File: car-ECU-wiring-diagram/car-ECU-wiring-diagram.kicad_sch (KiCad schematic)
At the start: 29 parts

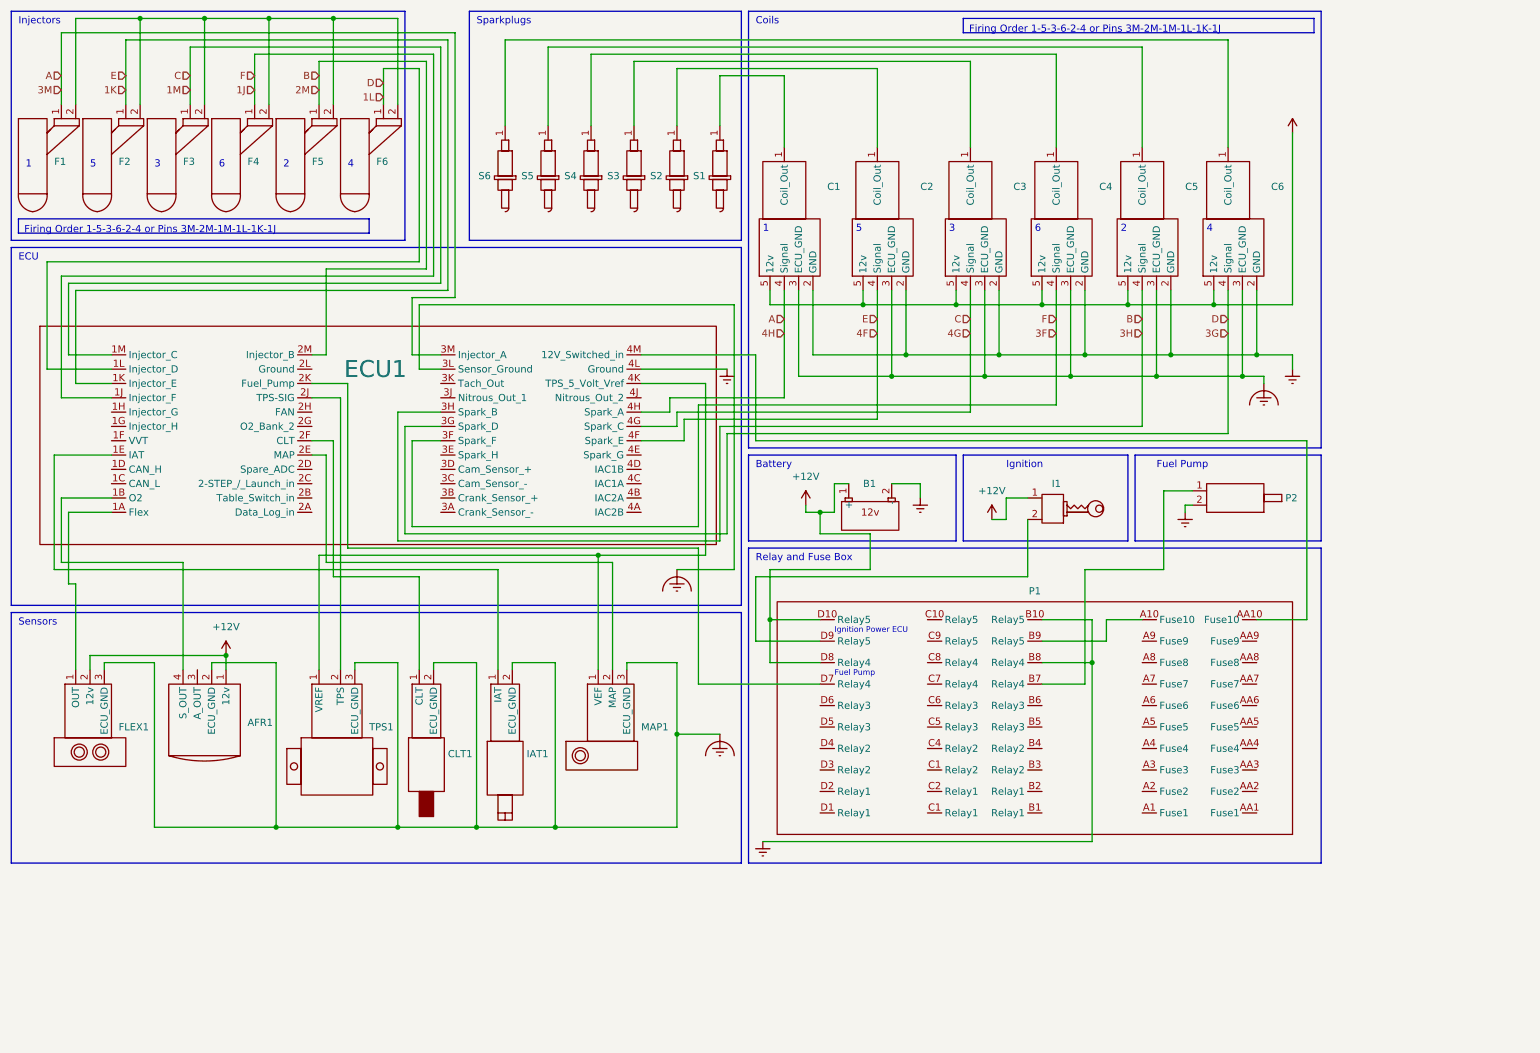
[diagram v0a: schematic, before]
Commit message: Update ECU wiring diagram with corrected pin UUIDs
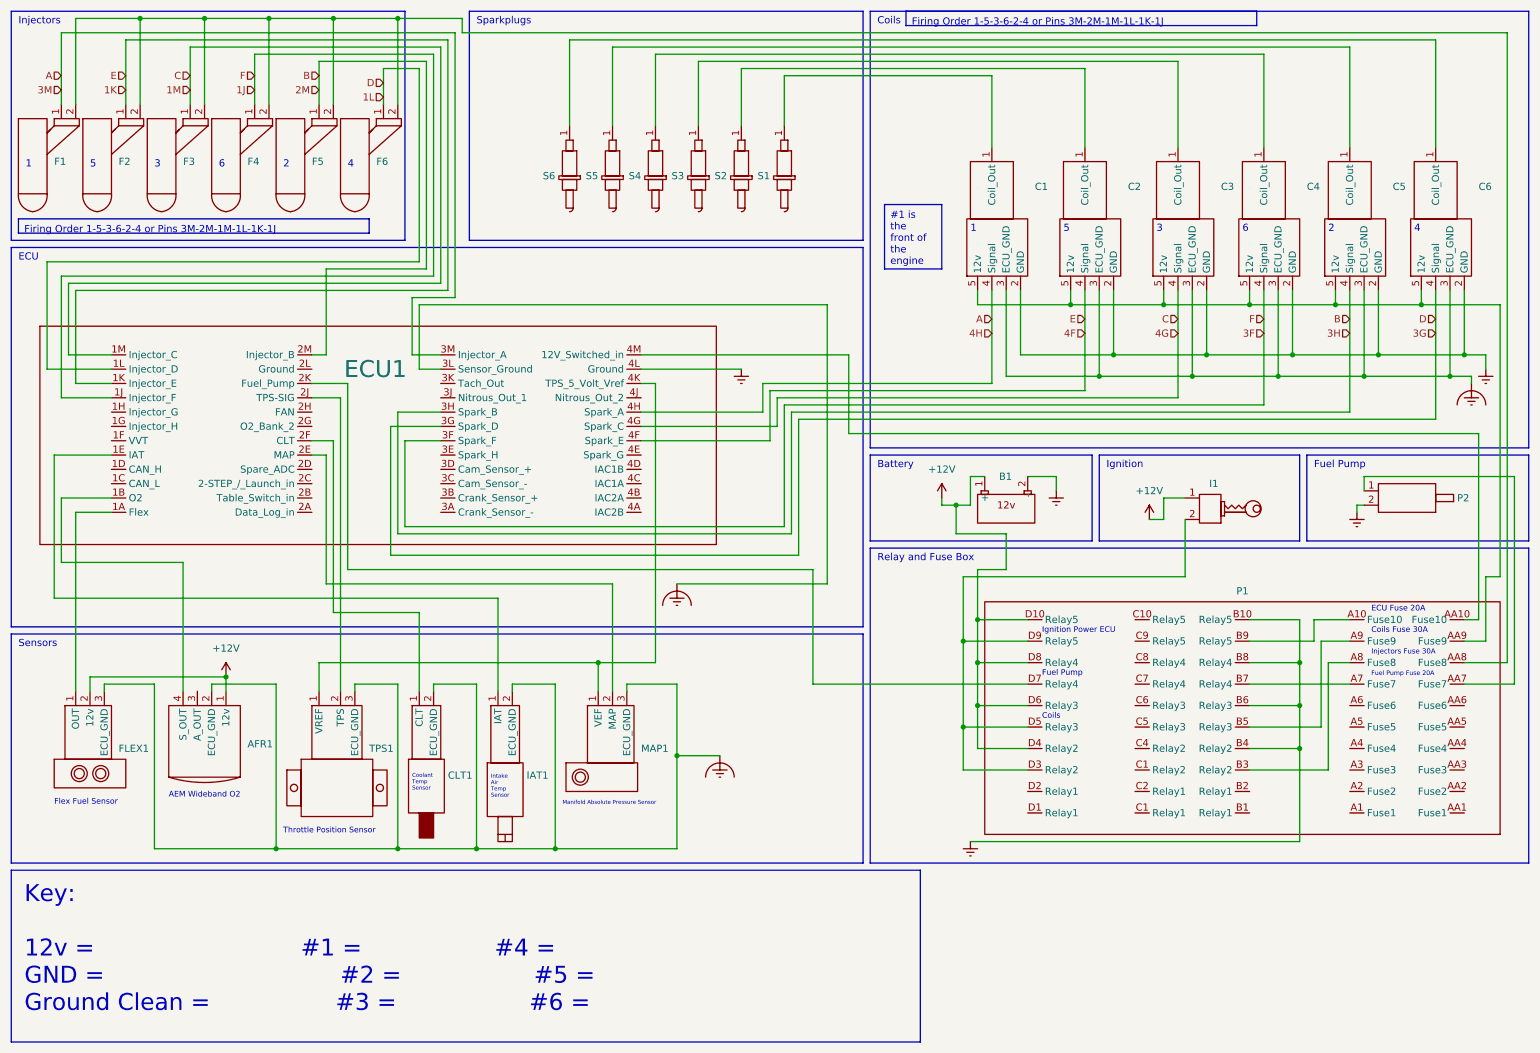
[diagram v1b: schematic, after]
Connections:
- net +12V: now also P1.D4 (Relay2), P1.D6 (Relay3); no longer C1.5 (12v), C2.5 (12v), C3.5 (12v), C4.5 (12v), C5.5 (12v), C6.5 (12v)
- net Earth: now also P1.B4 (Relay2), P1.B6 (Relay3)
- net at F1.2, F2.2, F3.2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: now also P1.AA8 (Fuse8)
- net at I1.2, P1.D9 (Relay5): now also P1.D3 (Relay2), P1.D5 (Relay3)
- net at P2.1: now also P1.AA7 (Fuse7); no longer P1.B7 (Relay4)
- net at P1.A7 (Fuse7): now also P1.B7 (Relay4)
- net at P1.A8 (Fuse8): now also P1.B3 (Relay2)
- net at P1.A9 (Fuse9): now also P1.B5 (Relay3)
- net at P1.AA9 (Fuse9): now also C1.5 (12v), C2.5 (12v), C3.5 (12v), C4.5 (12v), C5.5 (12v), C6.5 (12v)
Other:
- note added: "AEM Wideband O2"
- note added: "Coils Fuse 30A"
- note added: "Coolant Temp Sensor"
- note added: "ECU Fuse 20A"
- note added: "Flex Fuel Sensor"
- note added: "Fuel Pump Fuse 20A"
- note added: "Injectors Fuse 30A"
- note added: "Intake Air Temp Sensor"
- note added: "Manifold Absolute Pressure Sensor"
- note added: "Throttle Position Sensor"
- moved on the sheet: AFR1, B1, C1, C2, C3, C4, C5, C6, CLT1, FLEX1, I1, IAT1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

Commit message: Update Coils Fuse amperage and Pin UUIDs in car-ECU-wiring-diagram.kicad_sch
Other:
- note added: "Coils Fuse 10A"
- note removed: "Coils Fuse 30A"
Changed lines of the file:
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@@
     (effects (font (size 1.27 1.27)) (justify left bottom))
   )
-  (text "Coils Fuse 30A" (at 255.27 124.46 0)
+  (text "Coils Fuse 10A" (at 255.27 124.46 0)
     (effects (font (size 1 1)) (justify left bottom))
   )
